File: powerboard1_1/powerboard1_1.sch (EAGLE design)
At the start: 100 parts, among them Q1 IPP80P03P4L04AKSA1, U1 UWQ-12/20-T48NBS-C, U2 UWE-5/20-Q48NB-C, U3 UWE-3.3/30-Q48NB-C

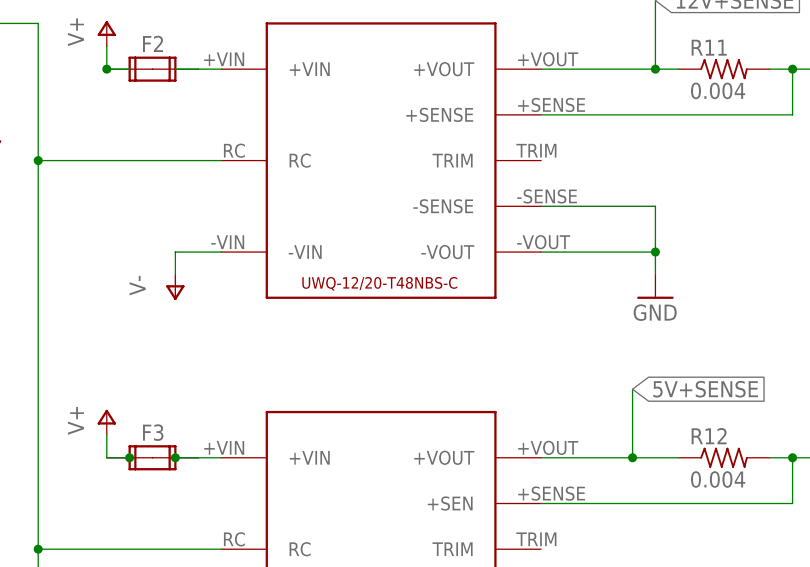
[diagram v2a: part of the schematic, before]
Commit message: Modified more traces and polygons; Fixed power board library
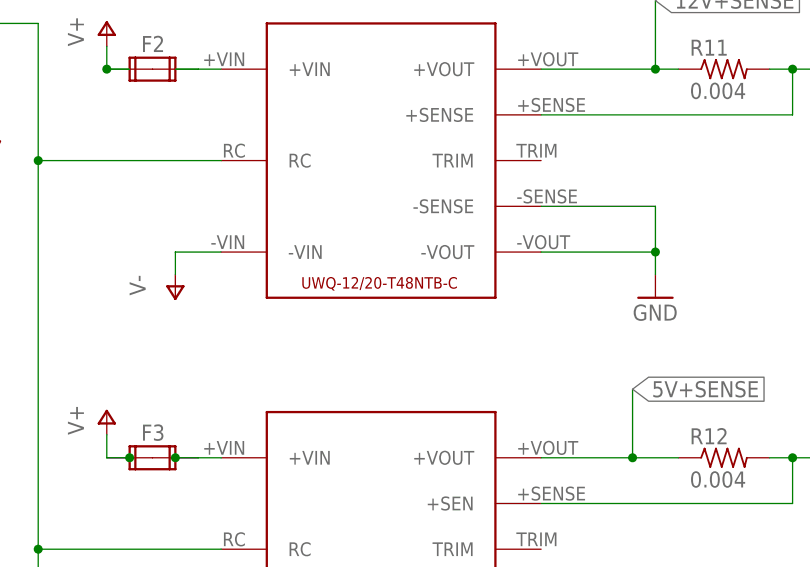
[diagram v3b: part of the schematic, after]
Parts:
- removed U1: UWQ-12/20-T48NBS-C, New Power Board Library:UWQ-12/20-T48NBS-C
- added U4: UWQ-12/20-T48NTB-C, New Power Board Library:UWQ-12/20-T48NTB-C
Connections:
- net 12V+SENSE: now also U4.+VOUT; no longer U1.+VOUT
- net 12V-SENSE: now also U4.+SENSE; no longer U1.+SENSE
- net GND: now also U4.-SENSE, U4.-VOUT; no longer U1.-SENSE, U1.-VOUT
- net N$5: now also U4.+VIN; no longer U1.+VIN
- net ON/OFF: now also U4.RC; no longer U1.RC
- net V-: now also U4.-VIN; no longer U1.-VIN
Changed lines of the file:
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@@
 <?xml version="1.0" encoding="utf-8"?>
 <!DOCTYPE eagle SYSTEM "eagle.dtd">
-<eagle version="8.0.1">
+<eagle version="8.0.2">
 <drawing>
 <settings>
@@
 <part name="P+3" library="supply1" deviceset="V+" device=""/>
 <part name="JP7" library="pinhead" deviceset="PINHD-1X2" device=""/>
-<part name="U1" library="New Power Board Library" deviceset="UWQ-12/20-T48NBS-C" device=""/>
 <part name="FRAME1" library="frames" deviceset="FRAME_A_L" device=""/>
 <part name="U2" library="New Power Board Library" deviceset="UWE-5/20-Q48NB-C" device=""/>
@@
 <part name="D1" library="diode" deviceset="BZV10" device=""/>
 <part name="C1" library="rcl" deviceset="CPOL-US" device="E3.5-8" value="100u"/>
+<part name="U4" library="New Power Board Library" deviceset="UWQ-12/20-T48NTB-C" device=""/>
 </parts>
 <sheets>
@@
 <instance part="P+3" gate="1" x="78.74" y="205.74"/>
 <instance part="JP7" gate="G$1" x="35.56" y="182.88" rot="R270"/>
-<instance part="U1" gate="G$1" x="129.54" y="218.44"/>
 <instance part="FRAME1" gate="G$1" x="5.08" y="53.34"/>
 <instance part="FRAME1" gate="G$2" x="177.8" y="53.34"/>
@@
 <attribute name="VALUE" x="54.991" y="216.916" size="1.778" layer="96" rot="R90"/>
 </instance>
+<instance part="U4" gate="G$1" x="129.54" y="218.44"/>
 </instances>
 <busses>
@@
 <pinref part="P-4" gate="1" pin="V-"/>
 <wire x1="106.68" y1="205.74" x2="106.68" y2="208.28" width="0.1524" layer="91"/>
-<pinref part="U1" gate="G$1" pin="-VIN"/>
 <wire x1="106.68" y1="208.28" x2="111.76" y2="208.28" width="0.1524" layer="91"/>
+<pinref part="U4" gate="G$1" pin="-VIN"/>
 </segment>
 <segment>
@@
 <pinref part="LED1" gate="G$1" pin="C"/>
 <wire x1="83.82" y1="223.52" x2="83.82" y2="233.68" width="0.1524" layer="91"/>
-<pinref part="U1" gate="G$1" pin="RC"/>
 <pinref part="U2" gate="G$1" pin="RC"/>
 <pinref part="U3" gate="G$1" pin="RC"/>
@@
 <wire x1="76.2" y1="241.3" x2="76.2" y2="233.68" width="0.1524" layer="91"/>
 <junction x="83.82" y="233.68"/>
+<pinref part="U4" gate="G$1" pin="RC"/>
 </segment>
 </net>
@@
 <wire x1="160.02" y1="208.28" x2="160.02" y2="205.74" width="0.1524" layer="91"/>
 <pinref part="GND4" gate="1" pin="GND"/>
-<pinref part="U1" gate="G$1" pin="-VOUT"/>
-<pinref part="U1" gate="G$1" pin="-SENSE"/>
 <wire x1="147.32" y1="213.36" x2="160.02" y2="213.36" width="0.1524" layer="91"/>
 <wire x1="160.02" y1="213.36" x2="160.02" y2="208.28" width="0.1524" layer="91"/>
 <junction x="160.02" y="208.28"/>
+<pinref part="U4" gate="G$1" pin="-VOUT"/>
+<pinref part="U4" gate="G$1" pin="-SENSE"/>
 </segment>
 <segment>
@@
 <segment>
 <wire x1="147.32" y1="228.6" x2="160.02" y2="228.6" width="0.1524" layer="91"/>
-<pinref part="U1" gate="G$1" pin="+VOUT"/>
 <label x="160.02" y="236.22" size="1.778" layer="95" xref="yes"/>
 <wire x1="160.02" y1="228.6" x2="162.56" y2="228.6" width="0.1524" layer="91"/>
@@
 <junction x="160.02" y="228.6"/>
 <pinref part="R11" gate="G$1" pin="1"/>
+<pinref part="U4" gate="G$1" pin="+VOUT"/>
 </segment>
 <segment>
@@
 <pinref part="F2" gate="G$1" pin="2A"/>
 <pinref part="F2" gate="G$1" pin="2B"/>
-<pinref part="U1" gate="G$1" pin="+VIN"/>
 <wire x1="109.22" y1="228.6" x2="111.76" y2="228.6" width="0.1524" layer="91"/>
+<pinref part="U4" gate="G$1" pin="+VIN"/>
 </segment>
 </net>
@@
 <segment>
 <wire x1="172.72" y1="228.6" x2="175.26" y2="228.6" width="0.1524" layer="91"/>
-<pinref part="U1" gate="G$1" pin="+SENSE"/>
 <wire x1="175.26" y1="228.6" x2="177.8" y2="228.6" width="0.1524" layer="91"/>
 <wire x1="147.32" y1="223.52" x2="175.26" y2="223.52" width="0.1524" layer="91"/>
@@
 <label x="177.8" y="228.6" size="1.778" layer="95" xref="yes"/>
 <pinref part="R11" gate="G$1" pin="2"/>
-</segment>
-<segment>
+<pinref part="U4" gate="G$1" pin="+SENSE"/>
+</segment>
+<segment>

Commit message: Replaced output rail terminals with filtering capacitors; Modified LED circuit; Modified traces and polygons
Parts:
- removed X2, X3, X4, X5: (no value), con-phoenix-254:MPT3
- added C5, C6, C7: (no value), rcl:CPOL-USE5-10.5
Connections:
- net 12V-SENSE: now also C5.+; no longer X2-1.1, X2-2.1, X2-3.1
- net 3V3-SENSE: now also C7.+; no longer X5-1.1, X5-2.1, X5-3.1
- net 5V-SENSE: now also C6.+; no longer X4-1.1, X4-2.1, X4-3.1
- net GND: now also C5.-, C6.-, C7.-; no longer X3-1.1, X3-2.1, X3-3.1
- net ON/OFF: no longer LED1.C
- net V-: now also LED1.C
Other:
- moved on the sheet: C1, CY1, CY2, D1, F1, JP7, LED1, Q1, R1, R5, R6, R7

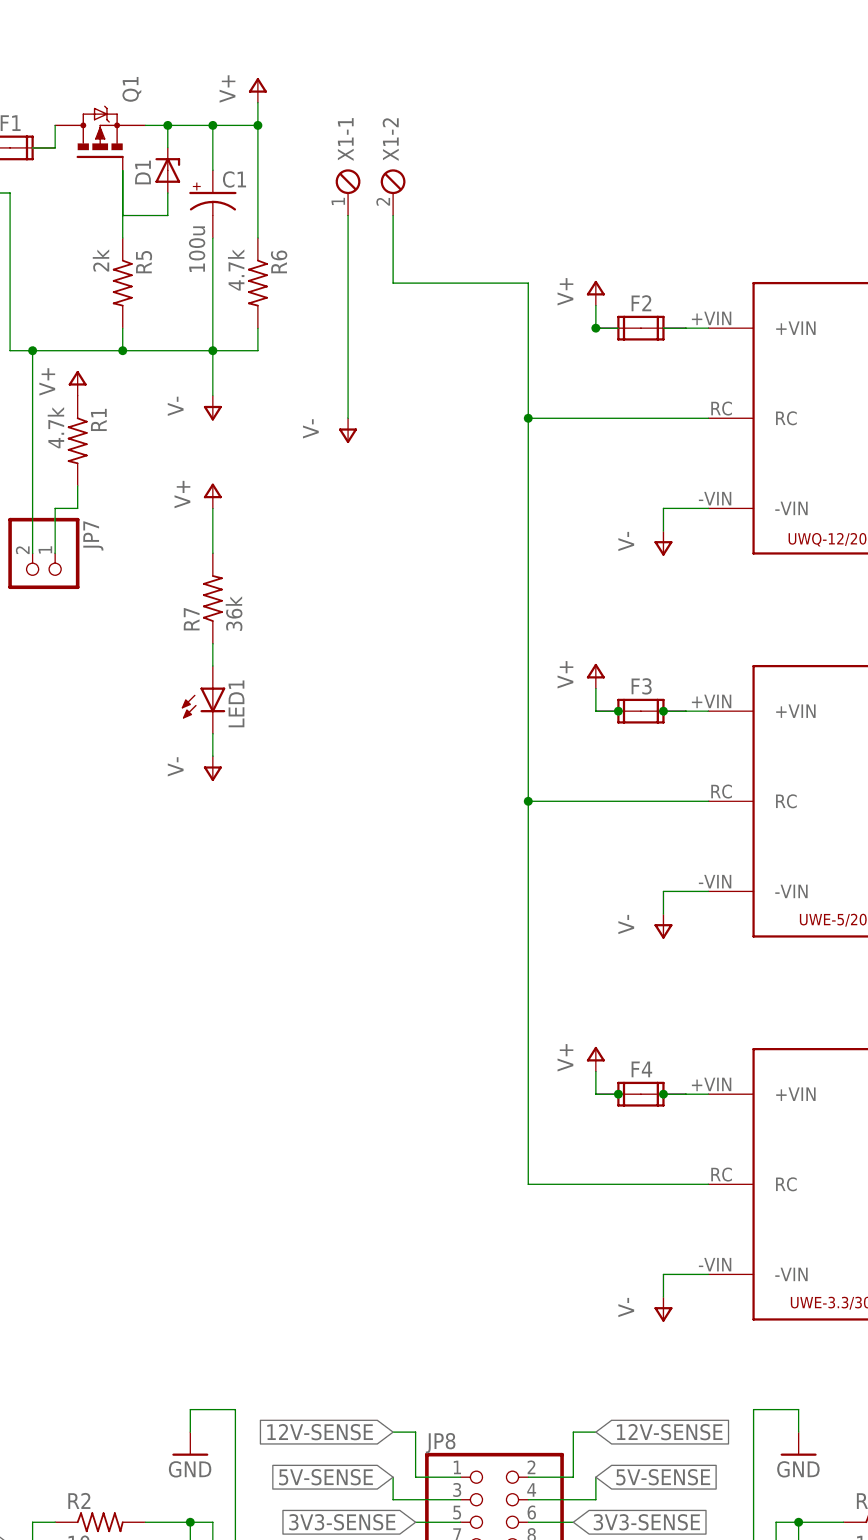
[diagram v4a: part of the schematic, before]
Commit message: Added open collector control circuit; Added input filtering capacitors
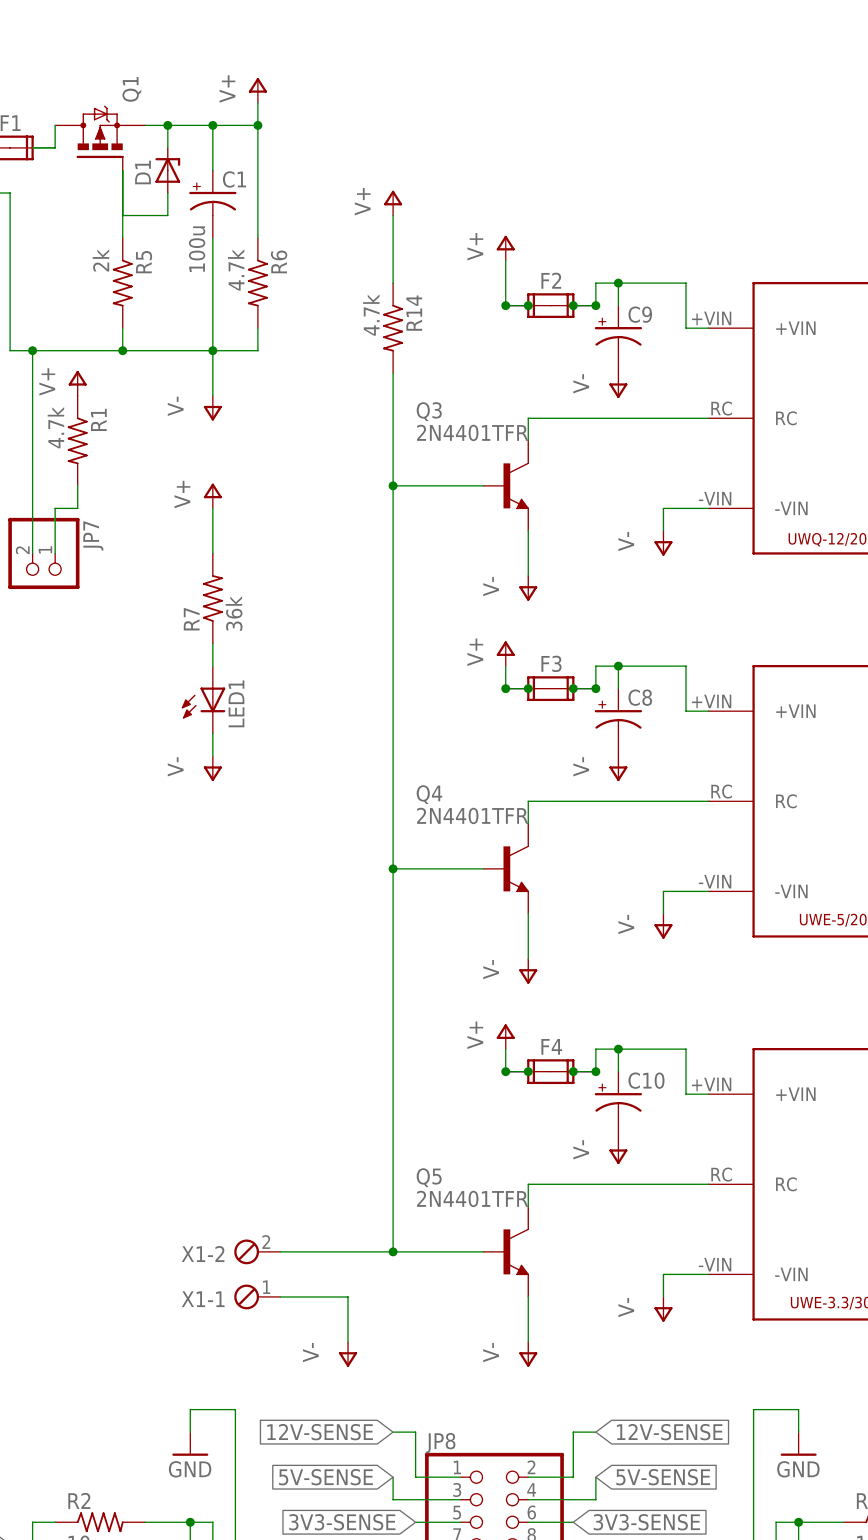
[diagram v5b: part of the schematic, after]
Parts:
- added C10, C8, C9: (no value), resistor:CPOL-USE2.5-7
- added Q3, Q4, Q5: 2N4401TFR, New Power Board Library:2N4401TFR
- added R14: 4.7k, resistor:R-US_0204/7
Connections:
- removed net N$6: F3.2A, F3.2B, U2.+VIN
- removed net N$7: F4.2A, F4.2B, U3.+VIN
- new net N$10: Q4.C, U2.RC
- new net N$11: Q5.C, U3.RC
- new net N$13: C10.+, F4.2A, F4.2B, U3.+VIN
- new net N$8: Q3.C, U4.RC
- new net N$9: C8.+, F3.2A, F3.2B, U2.+VIN
- net N$5: now also C9.+
- net ON/OFF: now also Q3.B, Q4.B, Q5.B, R14.2; no longer U2.RC, U3.RC, U4.RC
- net V+: now also R14.1
- net V-: now also C10.-, C8.-, C9.-, Q3.E, Q4.E, Q5.E
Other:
- moved on the sheet: F2, F3, F4, X1-1, X1-2

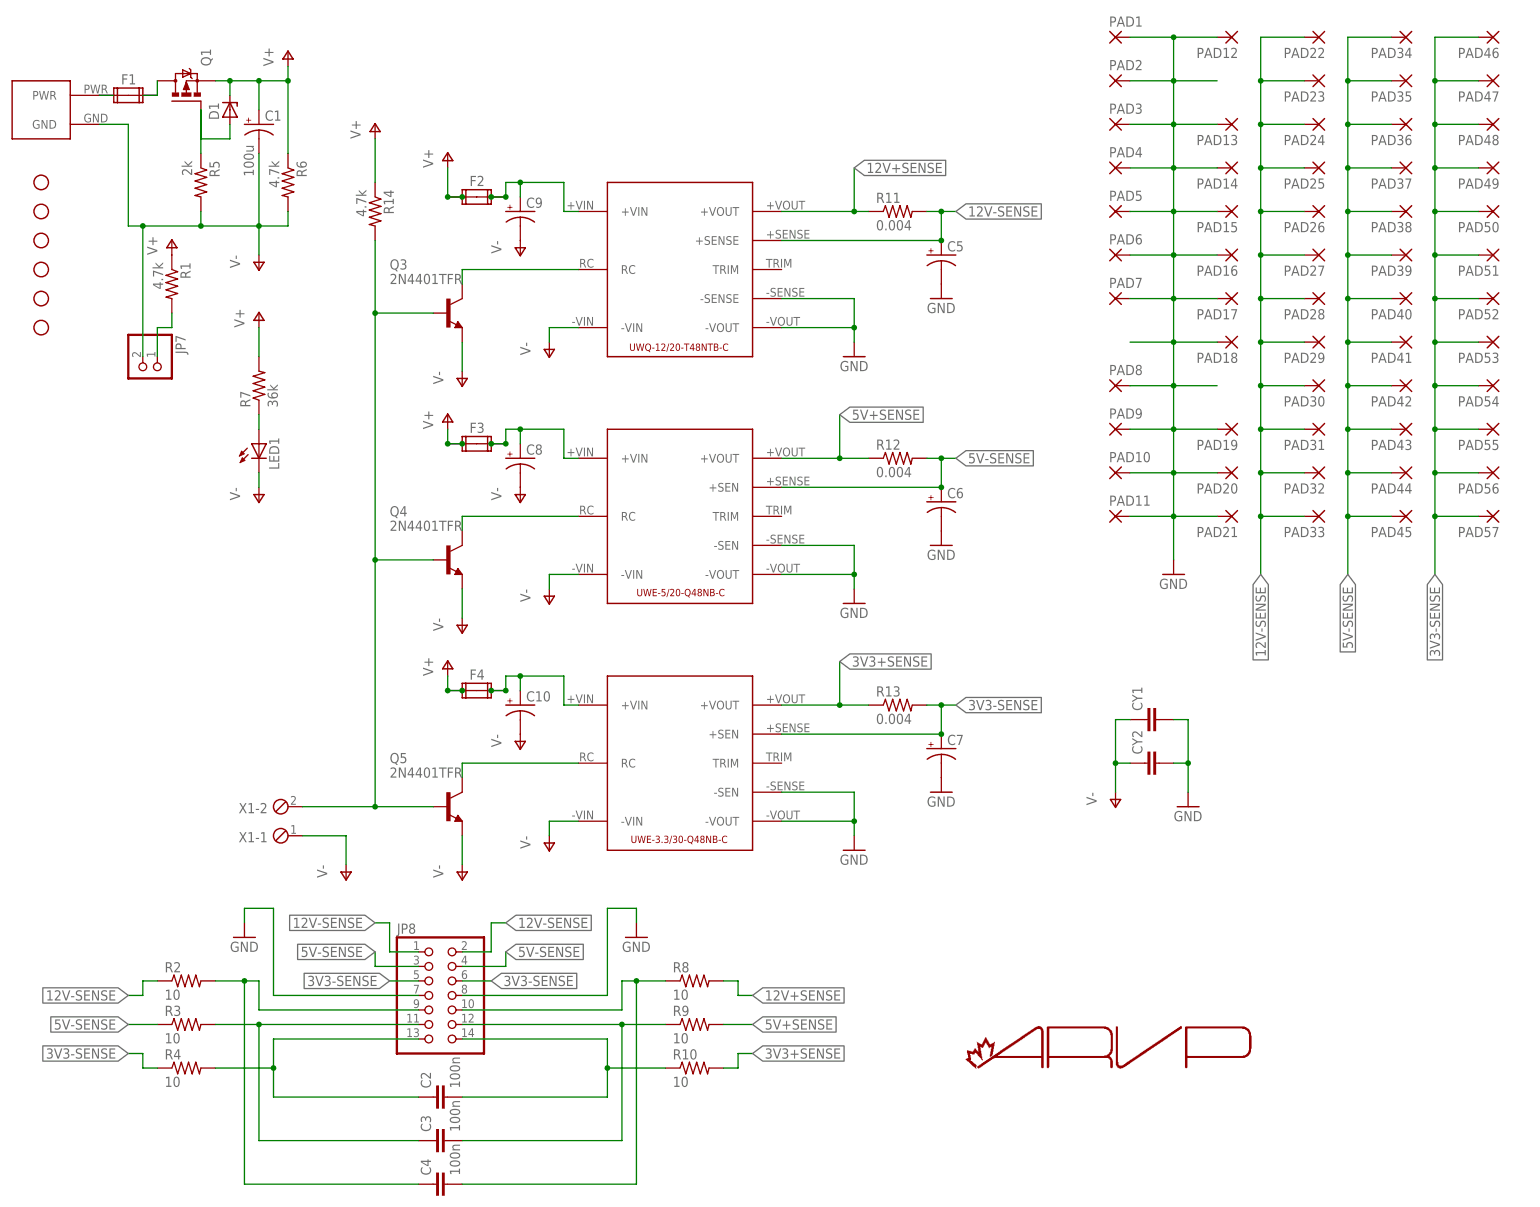
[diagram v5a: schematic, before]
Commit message: Modifed some routing, text/graphics positions
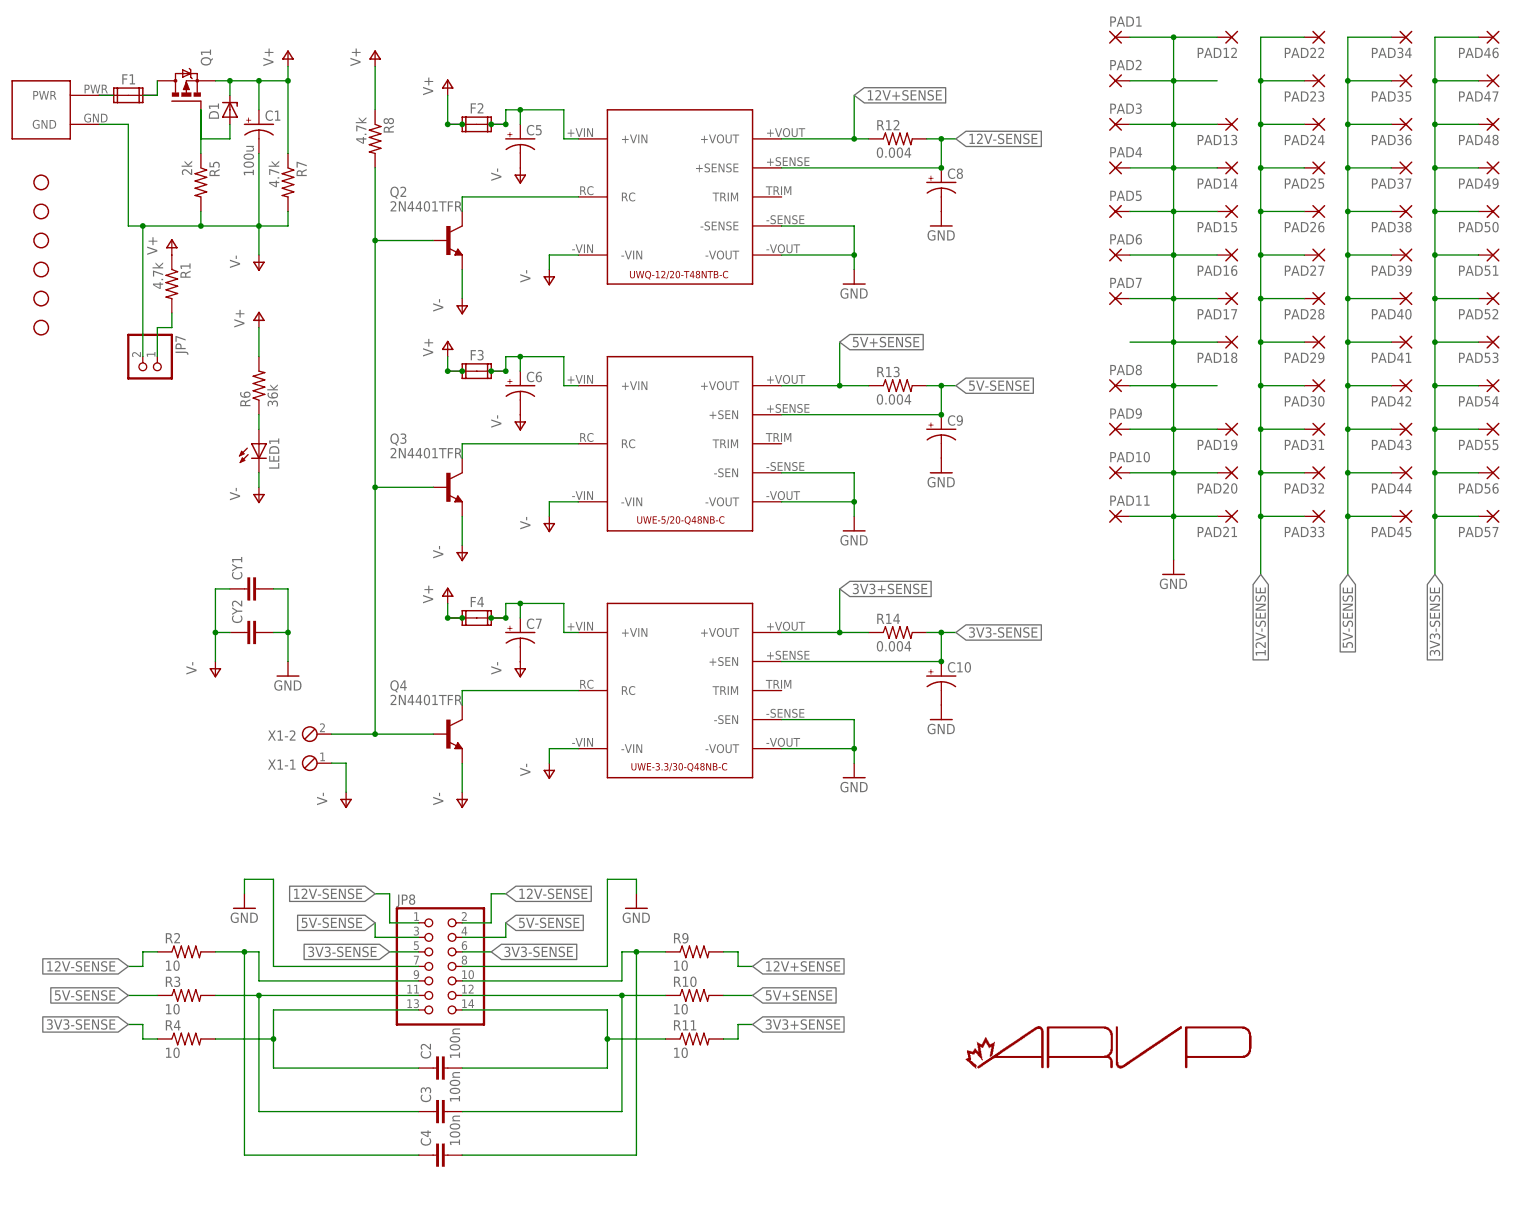
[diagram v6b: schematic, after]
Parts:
- removed Q5: 2N4401TFR, New Power Board Library:2N4401TFR
- removed U4: UWQ-12/20-T48NTB-C, New Power Board Library:UWQ-12/20-T48NTB-C
- added Q2: 2N4401TFR, New Power Board Library:2N4401TFR
- added U1: UWQ-12/20-T48NTB-C, New Power Board Library:UWQ-12/20-T48NTB-C
- C10, C8, C9: device resistor:CPOL-USE2.5-7 -> rcl:CPOL-USE5-10.5
- C5, C6, C7: device rcl:CPOL-USE5-10.5 -> rcl:CPOL-USE2.5-7
- R11: value 0.004 -> 10; device rcl:R-US_0617/22 -> rcl:R-US_0204/5
- R14: value 4.7k -> 0.004; device resistor:R-US_0204/7 -> rcl:R-US_0617/22
- R6: value 4.7k -> 36k
- R7: value 36k -> 4.7k
- R8: value 10 -> 4.7k; device rcl:R-US_0204/5 -> resistor:R-US_0204/7
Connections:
- net 12V+SENSE: now also R12.1, R9.2, U1.+VOUT; no longer R11.1, R8.2, U4.+VOUT
- net 12V-SENSE: now also C8.+, R12.2, U1.+SENSE; no longer C5.+, R11.2, U4.+SENSE
- net 3V3+SENSE: now also R11.2, R14.1; no longer R10.2, R13.1
- net 3V3-SENSE: now also C10.+, R14.2; no longer C7.+, R13.2
- net 5V+SENSE: now also R10.2, R13.1; no longer R12.1, R9.2
- net 5V-SENSE: now also C9.+, R13.2; no longer C6.+, R12.2
- net GND: now also C10.-, C8.-, C9.-, U1.-SENSE, U1.-VOUT; no longer C5.-, C6.-, C7.-, U4.-SENSE, U4.-VOUT
- net J4: now also R9.1; no longer R8.1
- net J6: now also R10.1; no longer R9.1
- net J8: now also R11.1; no longer R10.1
- net N$1: now also R6.1; no longer R7.1
- net N$10: now also Q3.C; no longer Q4.C
- net N$11: now also Q4.C; no longer Q5.C
- net N$13: now also C7.+; no longer C10.+
- net N$5: now also C5.+, U1.+VIN; no longer C9.+, U4.+VIN
- net N$8: now also Q2.C, U1.RC; no longer Q3.C, U4.RC
- net N$9: now also C6.+; no longer C8.+
- net ON/OFF: now also Q2.B, R8.2; no longer Q5.B, R14.2
- net V+: now also R6.2, R7.1, R8.1; no longer R14.1, R6.1, R7.2
- net V-: now also C5.-, C6.-, C7.-, Q2.E, R7.2, U1.-VIN; no longer C10.-, C8.-, C9.-, Q5.E, R6.2, U4.-VIN
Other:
- moved on the sheet: C10, C2, C3, C4, C5, C6, C7, C8, C9, CY1, CY2, F2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
